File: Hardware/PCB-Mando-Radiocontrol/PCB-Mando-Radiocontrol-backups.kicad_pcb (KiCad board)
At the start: 2 copper layers, 132 x 66 mm, 25 parts, among them J2 ALIMENTACION, J3 USB 2.0 a UART TTL 6 pines CP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, SW1 SW_SPDT, U1 ATMEGA328P, U2 Nrf24l01, U3 AMS1117-3.3, U4 AMS1117-5.0, U5 COM-09032, U6 COM-09032, Y1 16MHZ

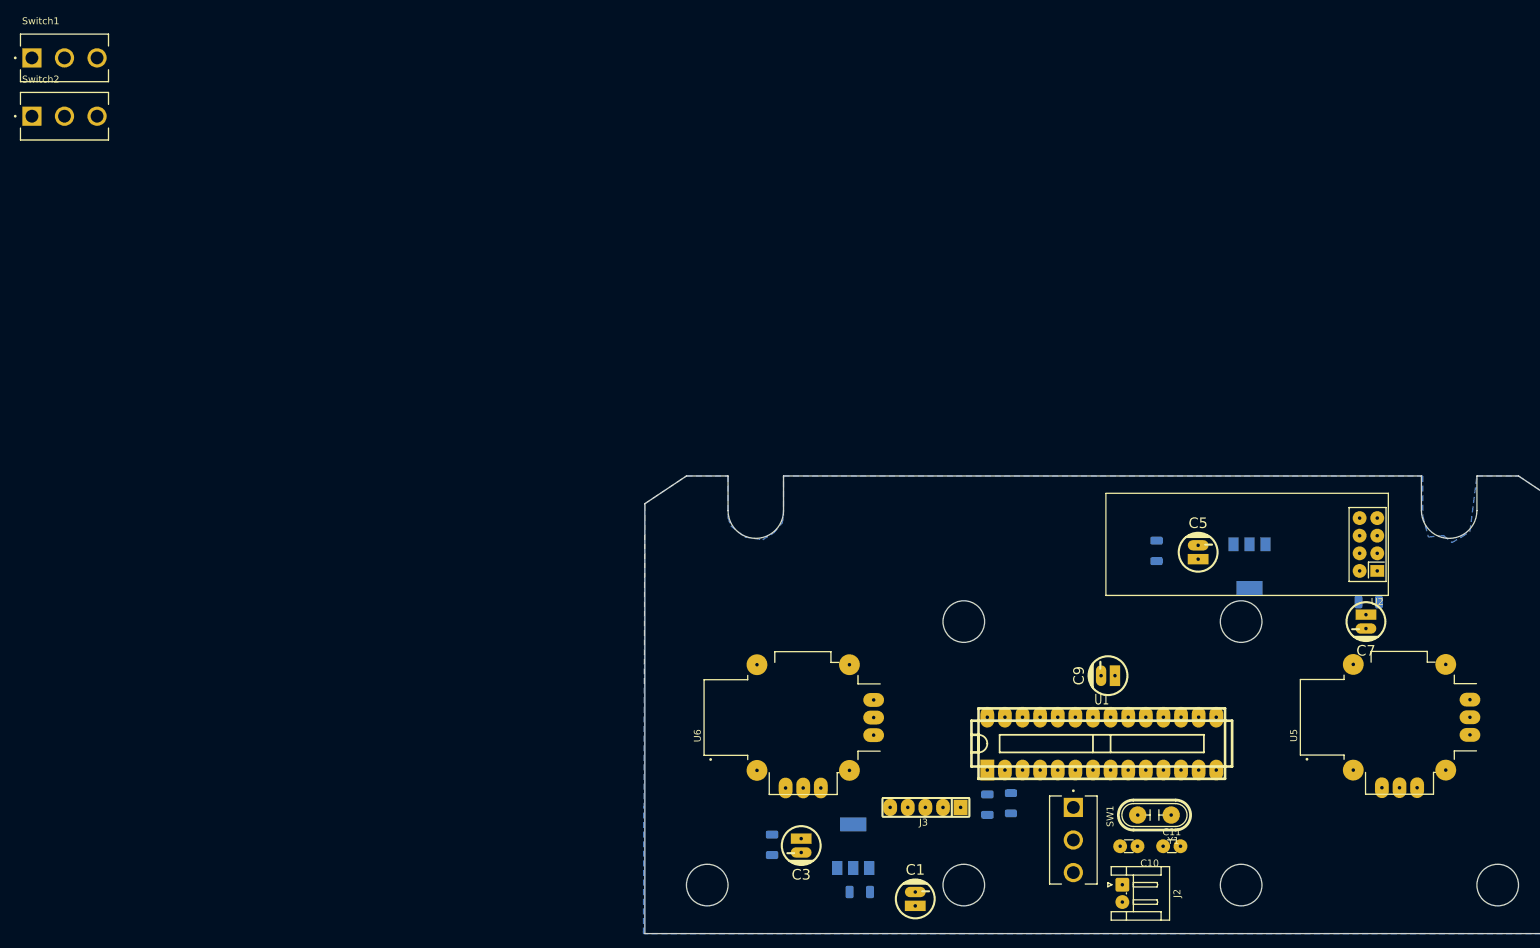
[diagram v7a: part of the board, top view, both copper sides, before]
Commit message: realice la base final de la placa , ordene cosas y cambie pines me falta agregar dos switches y ordenar y corroborar todo
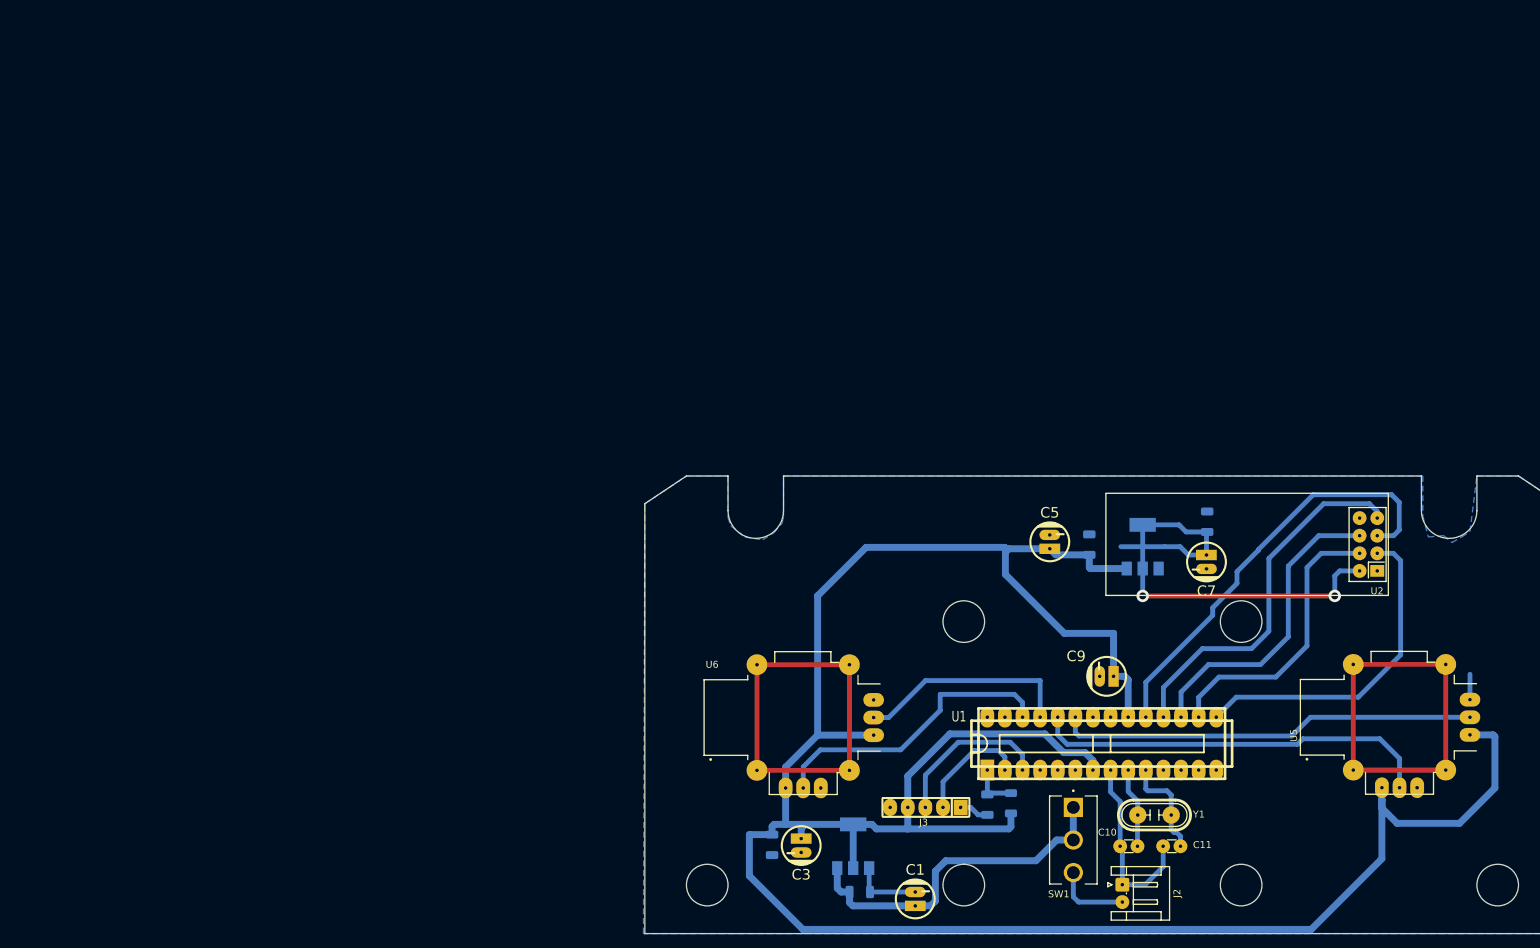
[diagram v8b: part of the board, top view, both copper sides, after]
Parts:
- removed Switch1, Switch2: ~, Footprints:SW_100SP3T1B1M2QE
- SW1: value SW_SPDT -> Encendido
- moved C8 26.0 mm to (172.1, 70.6), turned to 90 degrees
- moved C7 24.6 mm to (172.0, 76.4)
- moved C5 21.5 mm to (149.4, 73.5)
- moved U3 15.7 mm to (162.8, 74.2), turned to 90 degrees
- moved C6 9.74 mm to (155.1, 73.9)
- moved C9 0.22 mm to (157.6, 92.9)
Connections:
- U1 pad 25: /PotIzqB -> /PotIzqA
- U1 pad 26: /PotIzqA -> /PotIzqB
- U5 pad S1: Net-(U5-SHIELD-PadS1) -> GND
- U5 pad S2: Net-(U5-SHIELD-PadS1) -> GND
- U5 pad S3: Net-(U5-SHIELD-PadS1) -> GND
- U5 pad S4: Net-(U5-SHIELD-PadS1) -> GND
- U6 pad S1: Net-(U6-SHIELD-PadS1) -> GND
- U6 pad S2: Net-(U6-SHIELD-PadS1) -> GND
- U6 pad S3: Net-(U6-SHIELD-PadS1) -> GND
- U6 pad S4: Net-(U6-SHIELD-PadS1) -> GND
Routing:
- net +5V: track 0.97 -> 367.0 mm
- net GND: track 0.00 -> 155.1 mm
- net +3V3: track 0.00 -> 70.7 mm, vias 0 -> 2
- net /SCK: track 0.00 -> 62.5 mm
- net /PotDerA: track 0.00 -> 60.4 mm
- net /PotDerB: track 0.00 -> 58.1 mm
- net /MISO: track 0.00 -> 53.7 mm
- net VCC: track 0.00 -> 50.1 mm
- net /CE: track 0.00 -> 47.7 mm
- net /MOSI: track 0.00 -> 44.7 mm
- net /PotIzqB: track 0.00 -> 43.0 mm
- net /CSK: track 0.00 -> 41.3 mm
- net /PotIzqA: track 0.00 -> 31.5 mm
- net /TX: track 0.00 -> 23.6 mm
- net /RX: track 0.00 -> 16.8 mm
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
